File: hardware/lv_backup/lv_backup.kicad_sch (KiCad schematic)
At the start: 27 parts, among them U1 LTC3106

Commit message: lv backup hw update, usb interface hw update, MCU pinout spreadsheet
added spreadsheet for mapping / allocating MCU pins and resources

updated LV backup schematic with divider / buffer amplifier for MCU measurement

updated USB interface voltage buffers: all have high-impedance /2 buffers
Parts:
- added C8: 1u, Capacitor_SMD:C_0402_1005Metric_Pad0.74x0.62mm_HandSolder, symbol Device:C
- added R17, R18: 1Meg, Resistor_SMD:R_0402_1005Metric_Pad0.72x0.64mm_HandSolder, symbol Device:R_US
- added U2: AD8541, Package_TO_SOT_SMD:TSOT-23-5, symbol HPB_symbols:AD8541
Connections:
- net GND: now also C8.2, R18.2, U2.2 (V-)
- net V_{CELL}: now also U2.1, U2.4 (-); no longer BT1.1 (+), C2.1, U1.14 (ENVSTR), U1.19 (V_{STORE}), U1.20 (V_{CAP})
- net V_{OUT}: now also C8.1, U2.5 (V+)
- new net: R17.2, R18.1, U2.3 (+)
- new net BKUP_BATT: BT1.1 (+), C2.1, R17.1, U1.14 (ENVSTR), U1.19 (V_{STORE}), U1.20 (V_{CAP})
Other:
- note added: "Cell Voltage Buffer"

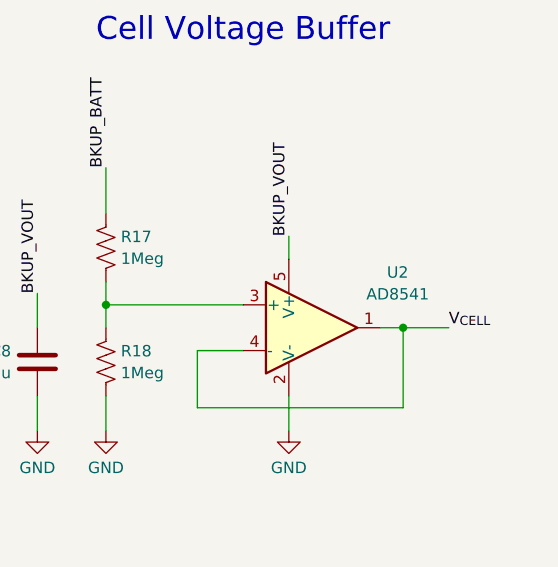
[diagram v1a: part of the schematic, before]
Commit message: hw amplifier change in lv backup and usb interface
replaced AD8541 operational amplifier with MCP6006 (massive cost savings, on order of $1 per chip or more)
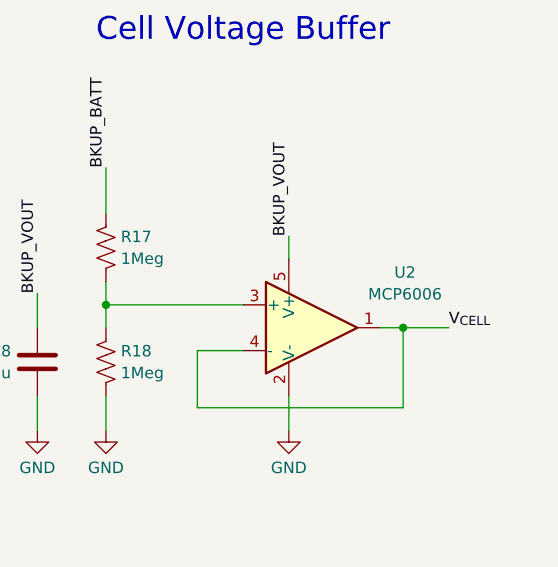
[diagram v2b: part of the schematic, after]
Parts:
- removed U2: AD8541, Package_TO_SOT_SMD:TSOT-23-5, symbol HPB_symbols:AD8541
- added U2: MCP6006, Package_TO_SOT_SMD:TSOT-23-5, symbol HPB_symbols:MCP6006
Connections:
- net GND: now also U2.2 (V-)
- net V_{CELL}: now also U2.1, U2.4 (-)
- net V_{OUT}: now also U2.5 (V+)
- net at R17.2, R18.1: now also U2.3 (+)
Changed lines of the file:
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@@
+	)
+	(symbol
+		(lib_id "HPB_symbols:MCP6006")
+		(at 250.19 71.12 0)
+		(unit 1)
+		(exclude_from_sim no)
+		(in_bom yes)
+		(on_board yes)
+		(dnp no)
+		(fields_autoplaced yes)
+		(property "Reference" "U2"
+			(at 260.5579 64.975 0)
+			(effects
+				(font
+					(size 1.27 1.27)
+				)
+			)
+		)
+		(property "Value" "MCP6006"
+			(at 260.5579 67.3993 0)
+			(effects
+				(font
+					(size 1.27 1.27)
+				)
+			)
+		)
+		(property "Footprint" "Package_TO_SOT_SMD:TSOT-23-5"
+			(at 250.19 71.12 0)
+			(effects
+				(font
+					(size 1.27 1.27)
+				)
+				(hide yes)
+			)
+		)
+		(property "Datasheet" "https://ww1.microchip.com/downloads/aemDocuments/documents/APID/ProductDocuments/DataSheets/MCP6006-6R-6U-7-9-Data-Sheet-20006411B.pdf"
+			(at 250.19 66.04 0)
+			(effects
+				(font
+					(size 1.27 1.27)
+				)
+				(hide yes)
+			)
+		)
+		(property "Description" "Amplifier, Operational, 1MHz, 5V, TSOT-23-5"
+			(at 250.19 71.12 0)
+			(effects
+				(font
+					(size 1.27 1.27)
+				)
+				(hide yes)
+			)
+		)
+		(pin "1"
+		)
+		(pin "4"
+		)
+		(pin "3"
+		)
+		(pin "5"
+		)
+		(pin "2"
+		)
+		(instances
+			(project ""
+				(path "/97f18045-69b9-43cc-8ecf-956eaff6dfdb"
+					(reference "U2")
+					(unit 1)
+				)
+			)
+		)
 	)
 	(symbol
@@
 					(unit 1)
 				)
-			)
-		)
-	)
-	(symbol
-		(lib_id "HPB_symbols:AD8541")
-		(at 250.19 71.12 0)
-		(unit 1)
-		(exclude_from_sim no)
-		(in_bom yes)
-		(on_board yes)
-		(dnp no)
-		(fields_autoplaced yes)
-		(property "Reference" "U2"
-			(at 259.7415 64.975 0)
-			(effects
-				(font
-					(size 1.27 1.27)
-				)
-			)
-		)
-		(property "Value" "AD8541"
-			(at 259.7415 67.3993 0)
-			(effects
-				(font
-					(size 1.27 1.27)
-				)
-			)
-		)
-		(property "Footprint" "Package_TO_SOT_SMD:TSOT-23-5"
-			(at 250.19 71.12 0)
-			(effects
-				(font
-					(size 1.27 1.27)
-				)
-				(hide yes)
-			)
-		)
-		(property "Datasheet" "https://www.analog.com/media/en/technical-documentation/data-sheets/ad8541_8542_8544.pdf"
-			(at 250.19 66.04 0)
-			(effects
-				(font
-					(size 1.27 1.27)
-				)
-				(hide yes)
-			)
-		)
-		(property "Description" "Precision Micropower, Low Noise CMOS, Rail-to-Rail Input/Output Operational Amplifier, TSOT-23-5"
-			(at 250.19 71.12 0)
-			(effects
-				(font
-					(size 1.27 1.27)
-				)
-				(hide yes)
-			)
-		)
-		(pin "2"
-		)
-		(pin "4"
-		)
-		(pin "1"
-		)
-		(pin "3"
-		)
-		(pin "5"
-		)
-		(instances
-			(project "lv_backup"
-				(path "/97f18045-69b9-43cc-8ecf-956eaff6dfdb"
-					(reference "U2")
-					(unit 1)
-				)
